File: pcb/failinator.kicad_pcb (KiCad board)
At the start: 2 copper layers, 200 x 124 mm, 82 parts, among them P1 CONN_01X04, P2 CONN_01X06, P3 CONN_01X06, P4 CONN_01X06, U1 74HC594, U2 RASPIPLUSHEADER, U3 LDS-CD16RI, U4 LDS-CD16RI, U5 74HC594

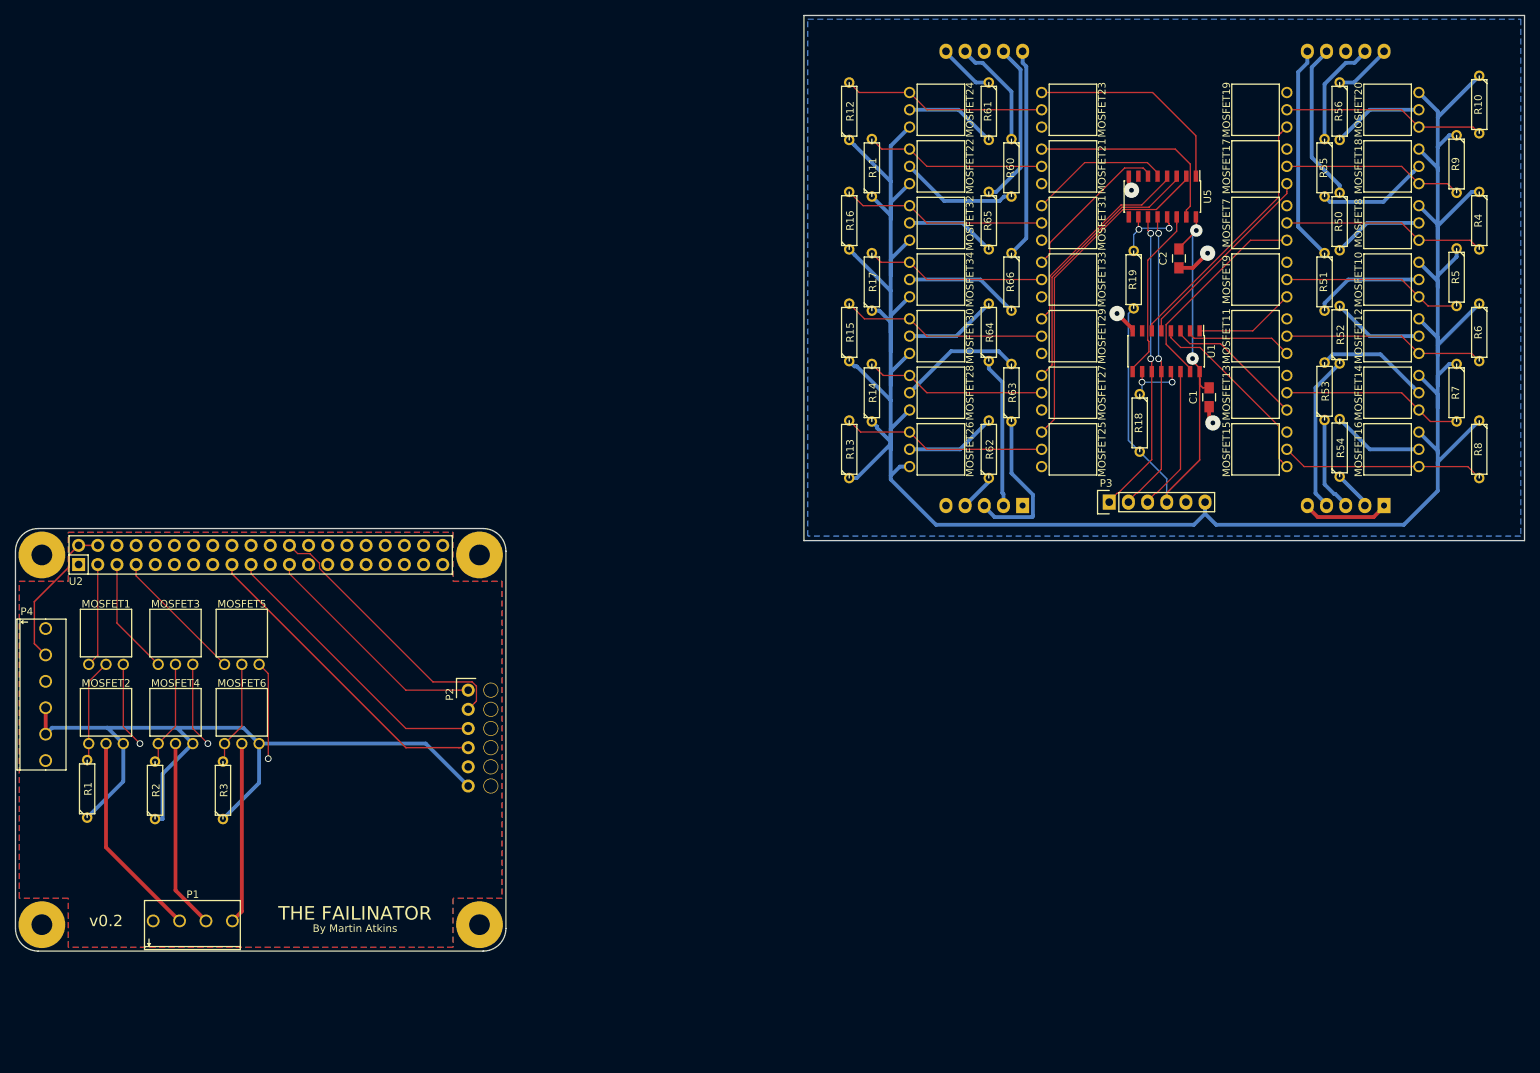
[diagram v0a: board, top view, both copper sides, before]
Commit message: Move the 7seg display board into a more sensible position
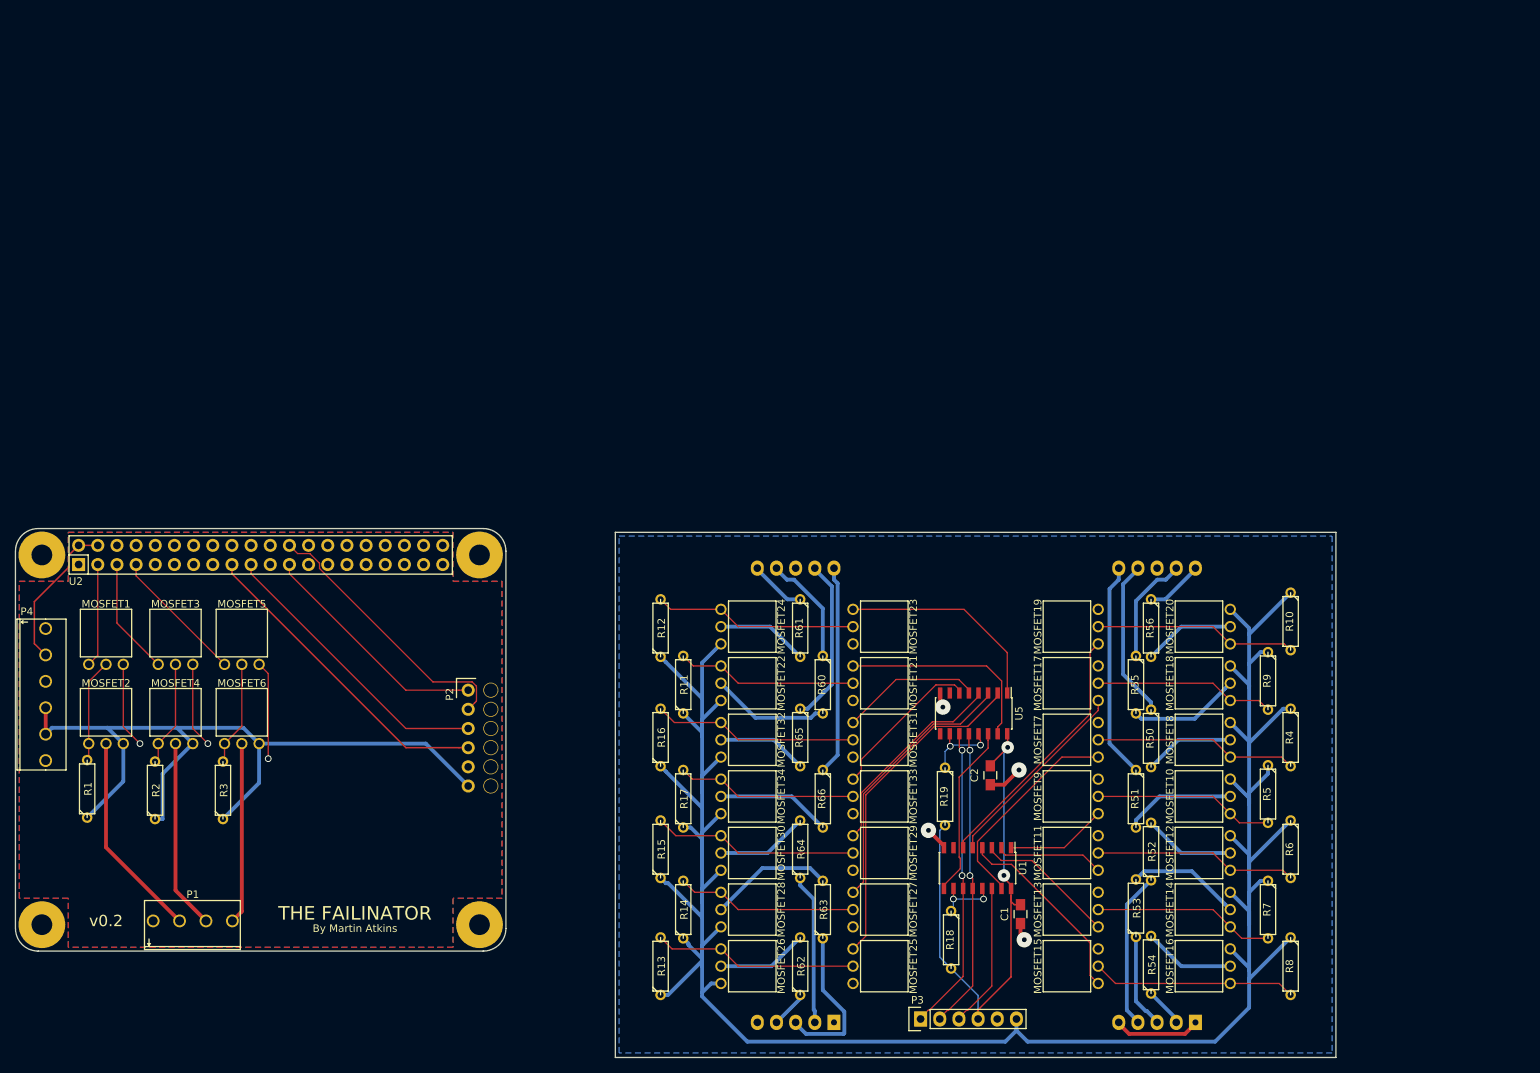
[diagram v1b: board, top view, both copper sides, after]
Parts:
- moved C1 72.9 mm to (228.7, 119.1)
- moved C2 72.9 mm to (224.7, 100.7)
- moved MOSFET10 72.9 mm to (256.5, 103.5)
- moved MOSFET11 72.9 mm to (239.0, 111.0)
- moved MOSFET12 72.9 mm to (256.5, 111.0)
- moved MOSFET13 72.9 mm to (239.0, 118.5)
- moved MOSFET14 72.9 mm to (256.5, 118.5)
- moved MOSFET15 72.9 mm to (239.0, 126.0)
- moved MOSFET16 72.9 mm to (256.5, 126.0)
- moved MOSFET17 72.9 mm to (239.0, 88.5)
- moved MOSFET18 72.9 mm to (256.5, 88.5)
- moved MOSFET19 72.9 mm to (239.0, 81.0)
- moved MOSFET20 72.9 mm to (256.5, 81.0)
- moved MOSFET21 72.9 mm to (206.5, 88.5)
- moved MOSFET22 72.9 mm to (189.0, 88.5)
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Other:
- board size 200 x 124 mm -> 175 x 70.1 mm

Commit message: Silkscreen title
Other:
- board text added: "LDS-CD16RI 7-SEGMENT LED DISPLAY DRIVER"
- board text added: "v0.1"
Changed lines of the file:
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@@
     (area 89.885286 -0.329001 296.029001 125.829)
     (thickness 1.6)
-    (drawings 16)
+    (drawings 19)
     (tracks 541)
     (zones 0)
@@
     )
   )
+  (gr_text v0.1 (at 223 77.5) (layer F.SilkS)
+    (effects (font (size 0.5 0.5) (thickness 0.125)))
+  )
+  (gr_text "By Martin Atkins" (at 223 76.5) (layer F.SilkS)
+    (effects (font (size 0.5 0.5) (thickness 0.125)))
+  )
+  (gr_text "LDS-CD16RI 7-SEGMENT\nLED DISPLAY DRIVER" (at 223 73.5) (layer F.SilkS)
+    (effects (font (size 1.5 1.5) (thickness 0.3)))
+  )
   (gr_line (start 270.5 68.5) (end 270.5 138.1) (layer Edge.Cuts) (width 0.1))

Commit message: Silkscreen labels for the various connections
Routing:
- added copper zone on F.Cu, net /DisplayDrivers/GND
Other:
- board text added: "+24V"
- board text added: "+3V3"
- board text added: "+5V"
- board text added: "B"
- board text added: "G"
- board text added: "GND"
- board text added: "MOSI"
- board text added: "R"
- board text added: "SCK"
- board text added: "~CS"
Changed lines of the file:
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@@
   (general
     (links 178)
-    (no_connects 0)
+    (no_connects 2)
     (area 89.885286 -0.329001 296.029001 125.829)
     (thickness 1.6)
-    (drawings 19)
+    (drawings 35)
     (tracks 541)
     (zones 0)
@@
   (module failinator:TERM_4 (layer F.Cu)
     (at 119 120)
-    (fp_text reference P1 (at 0 -3.5) (layer F.SilkS)
+    (fp_text reference P1 (at 7.5 3) (layer F.SilkS)
       (effects (font (size 1 1) (thickness 0.15)))
     )
@@
     (descr "Through hole pin header")
     (tags "pin header")
-    (fp_text reference P2 (at -2.45 0.55 90) (layer F.SilkS)
+    (fp_text reference P2 (at 0 -2.67 180) (layer F.SilkS)
       (effects (font (size 1 1) (thickness 0.15)))
     )
@@
     )
   )
+  (gr_text SCK (at 153 89.5 90) (layer F.SilkS)
+    (effects (font (size 0.5 0.5) (thickness 0.125)))
+  )
+  (gr_text ~CS (at 153 92 90) (layer F.SilkS)
+    (effects (font (size 0.5 0.5) (thickness 0.125)))
+  )
+  (gr_text MOSI (at 153 94.5 90) (layer F.SilkS)
+    (effects (font (size 0.5 0.5) (thickness 0.125)))
+  )
+  (gr_text +3V3 (at 153 97 90) (layer F.SilkS)
+    (effects (font (size 0.5 0.5) (thickness 0.125)))
+  )
+  (gr_text +24V (at 153 102 90) (layer F.SilkS)
+    (effects (font (size 0.5 0.5) (thickness 0.125)))
+  )
+  (gr_text GND (at 153 99.5 90) (layer F.SilkS)
+    (effects (font (size 0.5 0.5) (thickness 0.125)))
+  )
+  (gr_text GND (at 102.75 98.75 270) (layer F.SilkS)
+    (effects (font (size 0.5 0.5) (thickness 0.125)))
+  )
+  (gr_text +24V (at 102.75 95.25 270) (layer F.SilkS)
+    (effects (font (size 0.5 0.5) (thickness 0.125)))
+  )
+  (gr_text +24V (at 102.75 91.75 270) (layer F.SilkS)
+    (effects (font (size 0.5 0.5) (thickness 0.125)))
+  )
+  (gr_text GND (at 102.75 88.25 270) (layer F.SilkS)
+    (effects (font (size 0.5 0.5) (thickness 0.125)))
+  )
+  (gr_text +5V (at 102.75 84.75 270) (layer F.SilkS)
+    (effects (font (size 0.5 0.5) (thickness 0.125)))
+  )
+  (gr_text GND (at 102.75 81.25 270) (layer F.SilkS)
+    (effects (font (size 0.5 0.5) (thickness 0.125)))
+  )
+  (gr_text GND (at 113.75 116.5) (layer F.SilkS)
+    (effects (font (size 0.5 0.5) (thickness 0.125)))
+  )
+  (gr_text B (at 124.25 116.5) (layer F.SilkS)
+    (effects (font (size 0.5 0.5) (thickness 0.125)))
+  )
+  (gr_text G (at 120.75 116.5) (layer F.SilkS)
+    (effects (font (size 0.5 0.5) (thickness 0.125)))
+  )
+  (gr_text R (at 117.25 116.5) (layer F.SilkS)
+    (effects (font (size 0.5 0.5) (thickness 0.125)))
+  )
   (gr_text v0.1 (at 223 77.5) (layer F.SilkS)
     (effects (font (size 0.5 0.5) (thickness 0.125)))
@@
     (connect_pads (clearance 0.508))
     (min_thickness 0.254)
+    (fill yes (arc_segments 16) (thermal_gap 0.508) (thermal_bridge_width 0.508))
+    (polygon
+      (pts
+        (xy 175.5 69) (xy 270 69) (xy 270 137.5) (xy 175.5 137.5)
+      )
+    )
+  )
+  (zone (net 38) (net_name /DisplayDrivers/GND) (layer F.Cu) (hatch edge 0.508)
+    (connect_pads (clearance 0.508))
+    (min_thickness 0.254)

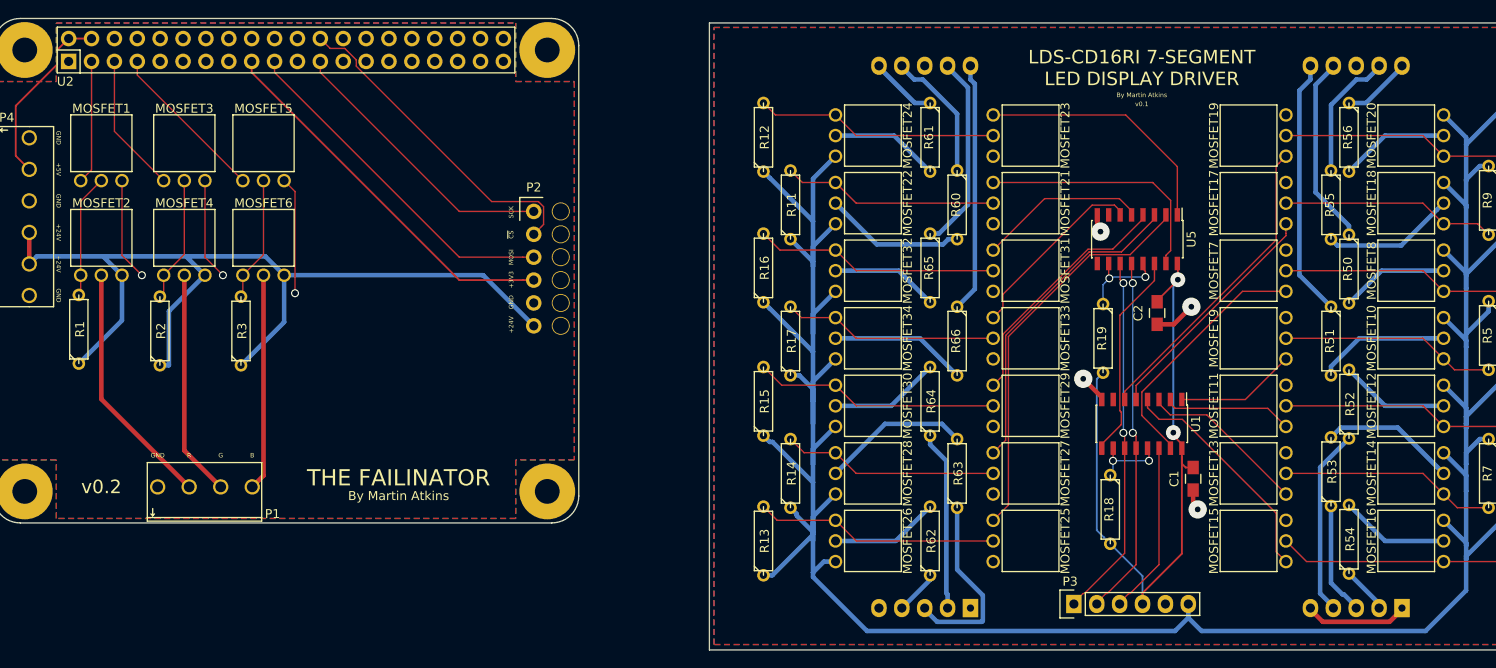
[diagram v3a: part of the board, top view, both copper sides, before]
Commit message: Possibly overboard on the silkscreen labels
The complete lack of labels last time made debugging difficult, so I'm
now going to the other extreme of labeling basically everything in case
we end up needing to attach probes or do more bodging this time around.
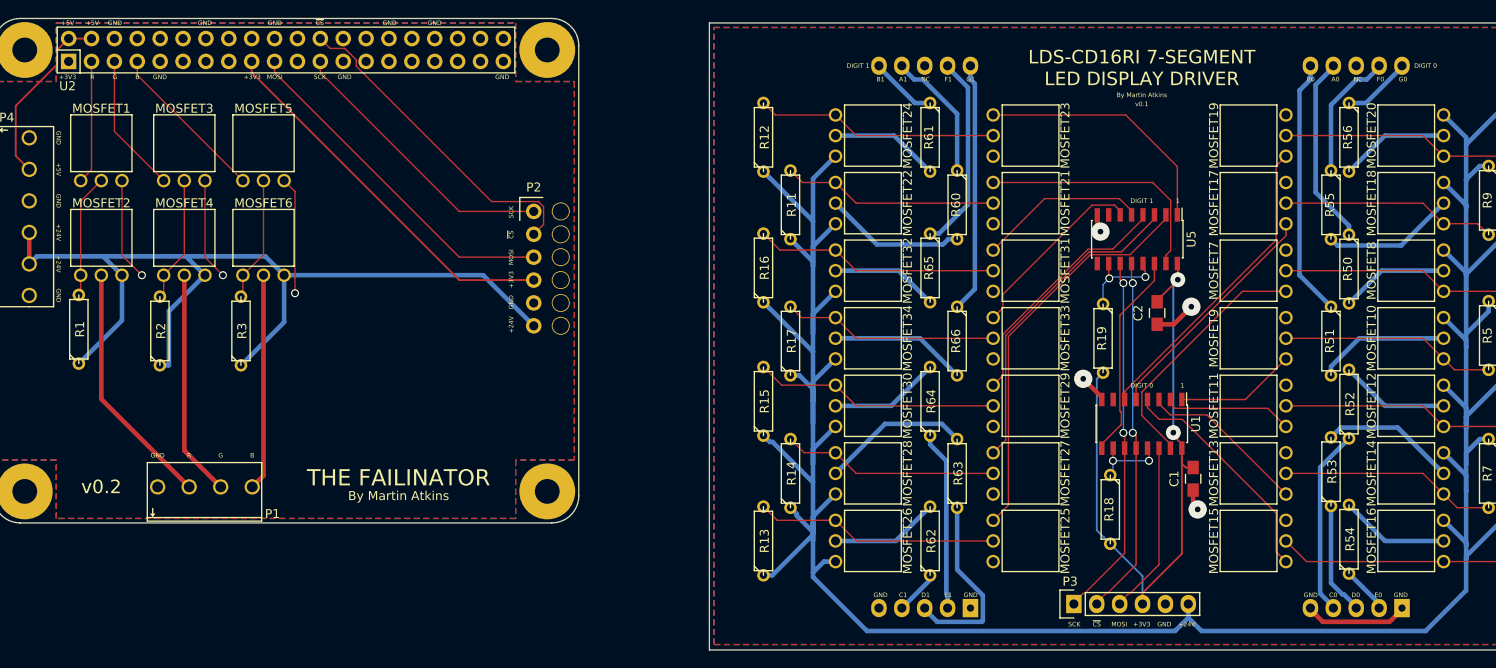
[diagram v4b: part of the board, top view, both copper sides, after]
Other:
- board text added: "1"
- board text added: "A0"
- board text added: "A1"
- board text added: "B0"
- board text added: "B1"
- board text added: "C0"
- board text added: "C1"
- board text added: "D0"
- board text added: "D1"
- board text added: "DIGIT 0"
- board text added: "DIGIT 1"
- board text added: "E0"
- board text added: "E1"
- board text added: "F0"
- board text added: "F1"
- board text added: "G0"
- board text added: "G1"
- board text added: "NC"
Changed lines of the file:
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@@
     (area 89.885286 -0.329001 296.029001 125.829)
     (thickness 1.6)
-    (drawings 35)
+    (drawings 87)
     (tracks 541)
     (zones 0)
@@
     (descr "Through hole pin header")
     (tags "pin header")
-    (fp_text reference U2 (at -24.5 3.5) (layer F.SilkS)
+    (fp_text reference U2 (at -24.25 4) (layer F.SilkS)
       (effects (font (size 1 1) (thickness 0.15)))
     )
@@
     )
   )
+  (gr_text "DIGIT 0" (at 263 73) (layer B.SilkS)
+    (effects (font (size 1.5 1.5) (thickness 0.125)) (justify mirror))
+  )
+  (gr_text "DIGIT 1" (at 182.5 72.5) (layer B.SilkS)
+    (effects (font (size 1.5 1.5) (thickness 0.125)) (justify mirror))
+  )
+  (gr_text "DIGIT 1" (at 191.5 73.25) (layer F.SilkS)
+    (effects (font (size 0.5 0.5) (thickness 0.125)))
+  )
+  (gr_text "DIGIT 0" (at 254.5 73.25) (layer F.SilkS)
+    (effects (font (size 0.5 0.5) (thickness 0.125)))
+  )
+  (gr_text "DIGIT 1" (at 223 88.25) (layer F.SilkS)
+    (effects (font (size 0.5 0.5) (thickness 0.125)))
+  )
+  (gr_text "DIGIT 0" (at 223 108.75) (layer F.SilkS)
+    (effects (font (size 0.5 0.5) (thickness 0.125)))
+  )
+  (gr_text G0 (at 252 74.75) (layer F.SilkS)
+    (effects (font (size 0.5 0.5) (thickness 0.125)))
+  )
+  (gr_text F0 (at 249.5 74.75) (layer F.SilkS)
+    (effects (font (size 0.5 0.5) (thickness 0.125)))
+  )
+  (gr_text NC (at 247 74.75) (layer F.SilkS)
+    (effects (font (size 0.5 0.5) (thickness 0.125)))
+  )
+  (gr_text A0 (at 244.5 74.75) (layer F.SilkS)
+    (effects (font (size 0.5 0.5) (thickness 0.125)))
+  )
+  (gr_text B0 (at 241.75 74.75) (layer F.SilkS)
+    (effects (font (size 0.5 0.5) (thickness 0.125)))
+  )
+  (gr_text G1 (at 204 74.75) (layer F.SilkS)
+    (effects (font (size 0.5 0.5) (thickness 0.125)))
+  )
+  (gr_text F1 (at 201.5 74.75) (layer F.SilkS)
+    (effects (font (size 0.5 0.5) (thickness 0.125)))
+  )
+  (gr_text NC (at 199 74.75) (layer F.SilkS)
+    (effects (font (size 0.5 0.5) (thickness 0.125)))
+  )
+  (gr_text A1 (at 196.5 74.75) (layer F.SilkS)
+    (effects (font (size 0.5 0.5) (thickness 0.125)))
+  )
+  (gr_text B1 (at 194 74.75) (layer F.SilkS)
+    (effects (font (size 0.5 0.5) (thickness 0.125)))
+  )
+  (gr_text GND (at 204 132 360) (layer F.SilkS)
+    (effects (font (size 0.5 0.5) (thickness 0.125)))
+  )
+  (gr_text E1 (at 201.5 132) (layer F.SilkS)
+    (effects (font (size 0.5 0.5) (thickness 0.125)))
+  )
+  (gr_text D1 (at 199 132) (layer F.SilkS)
+    (effects (font (size 0.5 0.5) (thickness 0.125)))
+  )
+  (gr_text C1 (at 196.5 132) (layer F.SilkS)
+    (effects (font (size 0.5 0.5) (thickness 0.125)))
+  )
+  (gr_text GND (at 194 132 360) (layer F.SilkS)
+    (effects (font (size 0.5 0.5) (thickness 0.125)))
+  )
+  (gr_text E0 (at 249.25 132) (layer F.SilkS)
+    (effects (font (size 0.5 0.5) (thickness 0.125)))
+  )
+  (gr_text D0 (at 246.75 132) (layer F.SilkS)
+    (effects (font (size 0.5 0.5) (thickness 0.125)))
+  )
+  (gr_text C0 (at 244.25 132) (layer F.SilkS)
+    (effects (font (size 0.5 0.5) (thickness 0.125)))
+  )
+  (gr_text GND (at 241.75 132 360) (layer F.SilkS)
+    (effects (font (size 0.5 0.5) (thickness 0.125)))
+  )
+  (gr_text GND (at 251.75 132 360) (layer F.SilkS)
+    (effects (font (size 0.5 0.5) (thickness 0.125)))
+  )
+  (gr_text 1 (at 227 88.25) (layer F.SilkS)
+    (effects (font (size 0.5 0.5) (thickness 0.125)))
+  )
+  (gr_text 1 (at 227.5 108.75) (layer F.SilkS)
+    (effects (font (size 0.5 0.5) (thickness 0.125)))
+  )
+  (gr_text +24V (at 228 135.25 360) (layer F.SilkS)
+    (effects (font (size 0.5 0.5) (thickness 0.125)))
+  )
+  (gr_text GND (at 225.5 135.25 360) (layer F.SilkS)
+    (effects (font (size 0.5 0.5) (thickness 0.125)))
+  )
+  (gr_text +3V3 (at 223 135.25 360) (layer F.SilkS)
+    (effects (font (size 0.5 0.5) (thickness 0.125)))
+  )
+  (gr_text MOSI (at 220.5 135.25 360) (layer F.SilkS)
+    (effects (font (size 0.5 0.5) (thickness 0.125)))
+  )
+  (gr_text ~CS (at 218 135.25 360) (layer F.SilkS)
+    (effects (font (size 0.5 0.5) (thickness 0.125)))
+  )
+  (gr_text SCK (at 215.5 135.25 360) (layer F.SilkS)
+    (effects (font (size 0.5 0.5) (thickness 0.125)))
+  )
+  (gr_text B (at 111.5 74.5) (layer F.SilkS)
+    (effects (font (size 0.5 0.5) (thickness 0.125)))
+  )
+  (gr_text G (at 109 74.5) (layer F.SilkS)
+    (effects (font (size 0.5 0.5) (thickness 0.125)))
+  )
+  (gr_text R (at 106.5 74.5) (layer F.SilkS)
+    (effects (font (size 0.5 0.5) (thickness 0.125)))
+  )
+  (gr_text GND (at 144.5 68.5) (layer F.SilkS)
+    (effects (font (size 0.5 0.5) (thickness 0.125)))
+  )
+  (gr_text GND (at 139.5 68.5) (layer F.SilkS)
+    (effects (font (size 0.5 0.5) (thickness 0.125)))
+  )
+  (gr_text GND (at 134.5 74.5) (layer F.SilkS)
+    (effects (font (size 0.5 0.5) (thickness 0.125)))
+  )
+  (gr_text GND (at 119 68.5) (layer F.SilkS)
+    (effects (font (size 0.5 0.5) (thickness 0.125)))
+  )
+  (gr_text +5V (at 103.75 68.5) (layer F.SilkS)
+    (effects (font (size 0.5 0.5) (thickness 0.125)))
+  )
+  (gr_text +5V (at 106.5 68.5) (layer F.SilkS)
+    (effects (font (size 0.5 0.5) (thickness 0.125)))
+  )
+  (gr_text GND (at 109 68.5) (layer F.SilkS)
+    (effects (font (size 0.5 0.5) (thickness 0.125)))
+  )
+  (gr_text +3V3 (at 103.75 74.5) (layer F.SilkS)
+    (effects (font (size 0.5 0.5) (thickness 0.125)))
+  )
+  (gr_text GND (at 152 74.5) (layer F.SilkS)
+    (effects (font (size 0.5 0.5) (thickness 0.125)))
+  )
+  (gr_text GND (at 114 74.5) (layer F.SilkS)
+    (effects (font (size 0.5 0.5) (thickness 0.125)))
+  )
+  (gr_text GND (at 126.75 68.5) (layer F.SilkS)
+    (effects (font (size 0.5 0.5) (thickness 0.125)))
+  )
+  (gr_text +3V3 (at 124.25 74.5) (layer F.SilkS)
+    (effects (font (size 0.5 0.5) (thickness 0.125)))
+  )
+  (gr_text ~CS (at 131.75 68.5) (layer F.SilkS)
+    (effects (font (size 0.5 0.5) (thickness 0.125)))
+  )
+  (gr_text MOSI (at 126.75 74.5) (layer F.SilkS)
+    (effects (font (size 0.5 0.5) (thickness 0.125)))
+  )
+  (gr_text SCK (at 131.75 74.5 360) (layer F.SilkS)
+    (effects (font (size 0.5 0.5) (thickness 0.125)))
+  )
   (gr_text SCK (at 153 89.5 90) (layer F.SilkS)
